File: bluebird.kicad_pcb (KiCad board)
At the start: 2 copper layers, 99.8 x 99.7 mm, 89 parts, among them J1 USB_C_Receptacle_USB2.0, J2 Conn_01x02_Male, J3 Conn_01x05, J4 Conn_01x01, J5 Conn_01x01, J6 AVR-ISP-6, J7 Conn_01x04, SW1 SW_PUSH, U1 ATMEGA32U4, U2 MCP23017_SS, U3 IS31FL3731-SA, U4 PAM2401, U5 MCP73831-2-OT, Y1 FA328 16MHz

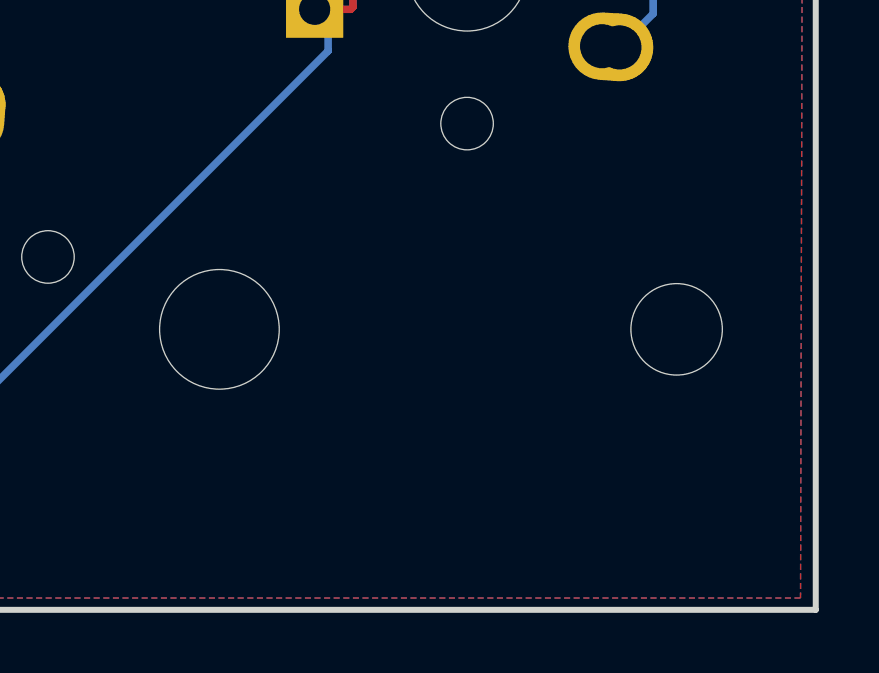
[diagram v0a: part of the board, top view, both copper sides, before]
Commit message: Add OSHW logo
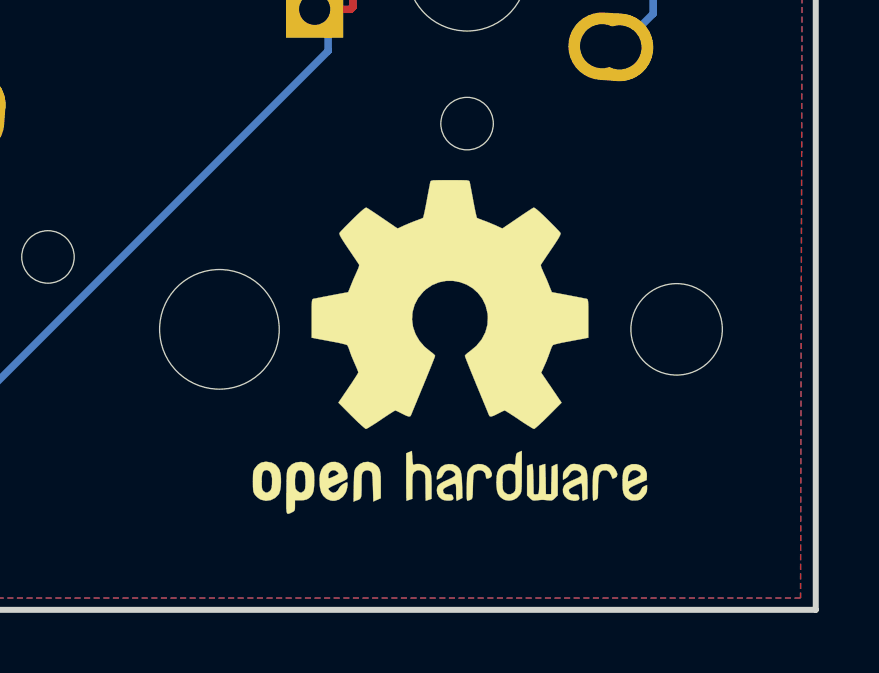
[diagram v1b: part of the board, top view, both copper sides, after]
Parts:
- added REF**: OSHW-Logo2_14.6x12mm_SilkScreen, Symbol:OSHW-Logo2_14.6x12mm_SilkScreen, F.Cu at (104.6, 109.5)
